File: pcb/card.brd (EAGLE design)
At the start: 84.8 x 54 mm, 18 parts, among them IC1 74HC14D, IC2 W25X32, Q1 BC817

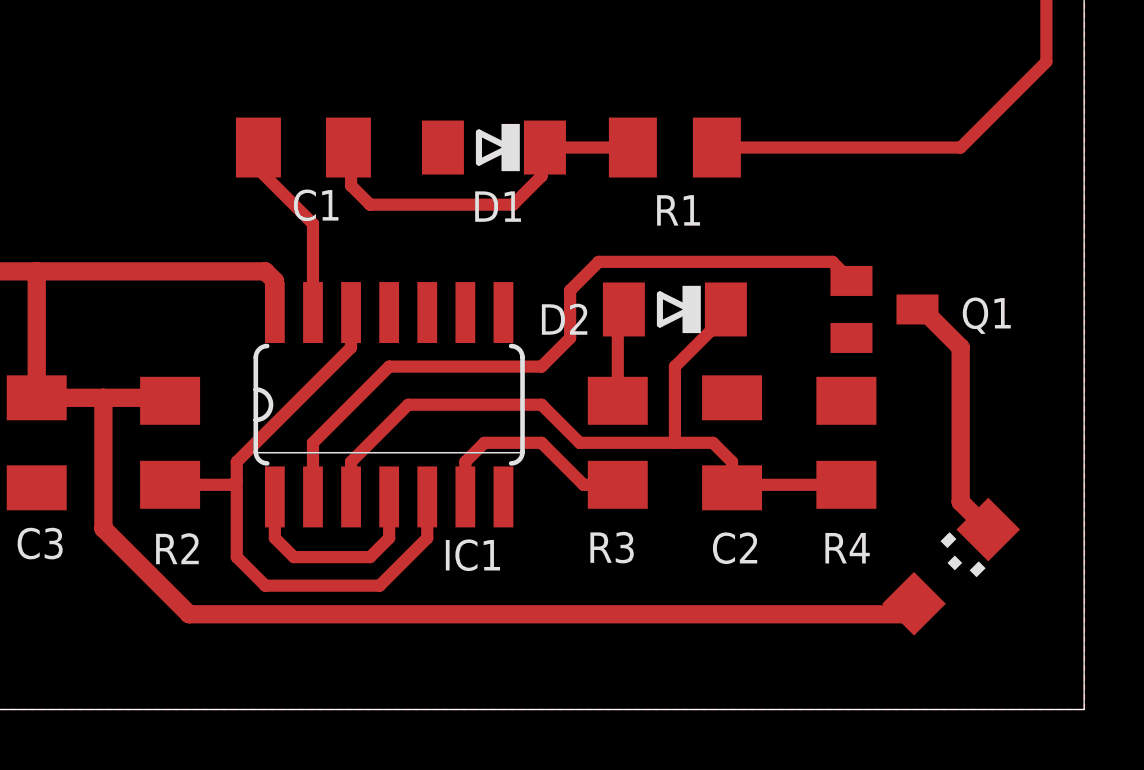
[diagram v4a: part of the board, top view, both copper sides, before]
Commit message: Added a current limitting resistor to the LED.
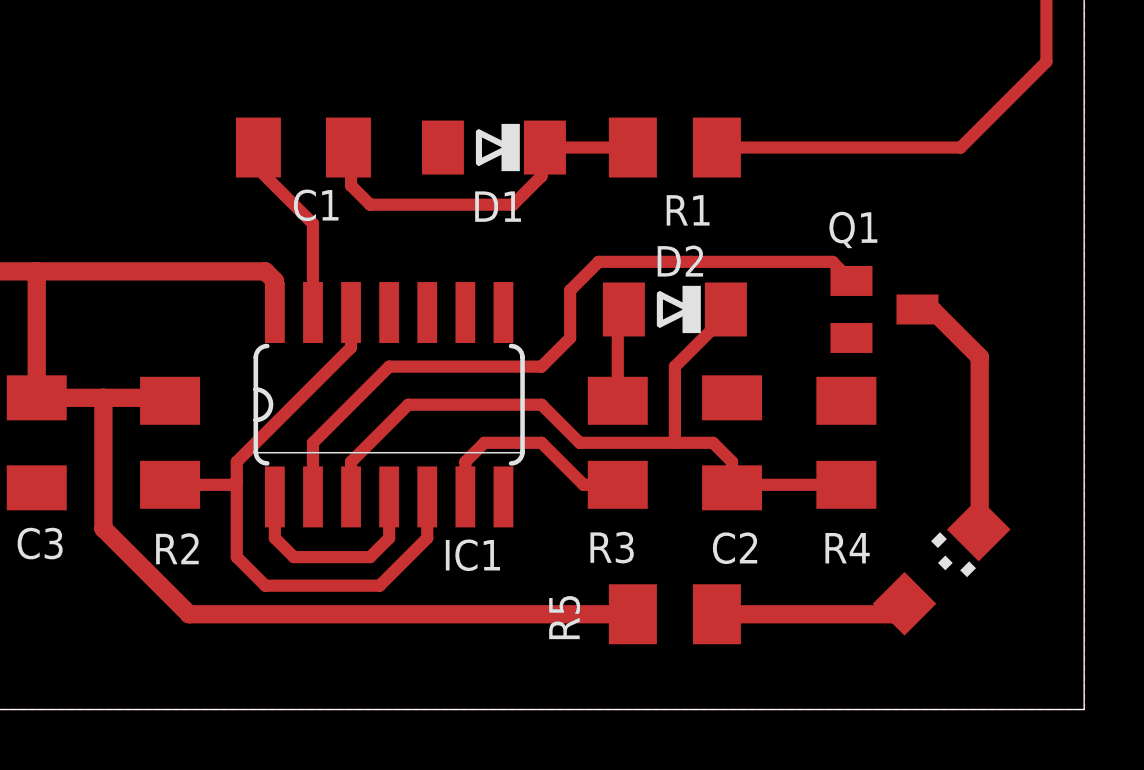
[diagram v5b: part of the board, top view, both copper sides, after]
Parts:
- added R5: 470R, resistor:M1206
- moved LED 0.32 mm to (80.0, 4.76)
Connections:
- new net N$3: LED.A, R5.2
- net VCC: now also R5.1; no longer LED.A
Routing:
- net VCC: track 77.7 -> 67.9 mm
- net N$3: track 0.00 -> 6.40 mm
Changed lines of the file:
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@@
 </element>
 <element name="D2" library="diode" package="MINIMELF" value="" x="71.12" y="13.335" smashed="yes" rot="R180">
-<attribute name="NAME" x="68.326" y="13.509515625" size="1.016" layer="25" rot="R180"/>
+<attribute name="NAME" x="70.4215" y="14.430484375" size="1.016" layer="25"/>
 <attribute name="VALUE" x="72.771" y="15.748" size="1.27" layer="27" rot="R180"/>
 </element>
@@
 <attribute name="NAME" x="65.405" y="5.6515" size="1.016" layer="25" ratio="10" rot="R180"/>
 </element>
-<element name="LED" library="led" package="CHIPLED_1206" value="" x="80.3275" y="4.7625" smashed="yes" rot="R315">
-<attribute name="VALUE" x="81.225525" y="2.068425" size="1.27" layer="27" rot="R45"/>
+<element name="LED" library="led" package="CHIPLED_1206" value="" x="80.01" y="4.7625" smashed="yes" rot="R315">
+<attribute name="VALUE" x="80.908021875" y="2.068425" size="1.27" layer="27" rot="R45"/>
 </element>
 <element name="Q1" library="transistor" package="SOT23-BEC" value="BC817" x="78.105" y="13.335" smashed="yes" rot="R270">
-<attribute name="NAME" x="80.645" y="12.7" size="1.016" layer="25"/>
+<attribute name="NAME" x="76.2" y="15.5575" size="1.016" layer="25"/>
 </element>
 <element name="R1" library="resistor" package="M1206" value="470k" x="71.12" y="18.7325" smashed="yes">
-<attribute name="NAME" x="72.0725" y="17.145" size="1.016" layer="25" rot="R180"/>
+<attribute name="NAME" x="72.39" y="17.145" size="1.016" layer="25" rot="R180"/>
 </element>
 <element name="R3" library="resistor" package="M1206" value="100k" x="69.215" y="8.89" smashed="yes" rot="R270">
@@
 <attribute name="NAME" x="66.1035" y="17.272" size="1.016" layer="25" rot="R180"/>
 <attribute name="VALUE" x="66.7385" y="21.1455" size="1.27" layer="27" rot="R180"/>
+</element>
+<element name="R5" library="resistor" package="M1206" value="470R" x="71.12" y="3.175" smashed="yes">
+<attribute name="NAME" x="67.945" y="2.2225" size="1.016" layer="25" rot="R90"/>
 </element>
 </elements>
@@
 <contactref element="IC1" pad="14"/>
 <contactref element="R2" pad="2"/>
-<contactref element="LED" pad="A"/>
 <contactref element="C3" pad="2"/>
 <wire x1="57.785" y1="12.7" x2="57.785" y2="13.2334" width="0.4064" layer="1"/>
 <contactref element="BAT" pad="+@2" route="any" routetag="G$1.+"/>
 <contactref element="BAT" pad="+@1" route="any" routetag="G$1.+"/>
-<wire x1="79.122625" y1="3.175" x2="79.0900625" y2="3.5250625" width="0.4064" layer="1"/>
 <contactref element="IC2" pad="8"/>
 <contactref element="IC2" pad="7"/>
@@
 <wire x1="52.07" y1="10.39" x2="54.1925" y2="10.39" width="0.6096" layer="1"/>
 <wire x1="54.1925" y1="10.39" x2="54.2925" y2="10.29" width="0.6096" layer="1"/>
-<wire x1="79.122625" y1="3.175" x2="54.9275" y2="3.175" width="0.6096" layer="1"/>
 <wire x1="54.9275" y1="3.175" x2="52.07" y2="6.0325" width="0.6096" layer="1"/>
 <wire x1="52.07" y1="6.0325" x2="52.07" y2="10.39" width="0.6096" layer="1"/>
+<contactref element="R5" pad="1"/>
+<wire x1="69.72" y1="3.175" x2="54.9275" y2="3.175" width="0.6096" layer="1"/>
 </signal>
 <signal name="N$2">
@@
 <wire x1="67.6275" y1="13.97" x2="68.58" y2="14.9225" width="0.4064" layer="1"/>
 </signal>
-<signal name="N$13">
-<contactref element="Q1" pad="C"/>
-<contactref element="LED" pad="C"/>
-<wire x1="79.205" y1="13.335" x2="79.375" y2="13.335" width="0.4064" layer="1"/>
-<wire x1="79.375" y1="13.335" x2="80.645" y2="12.065" width="0.6096" layer="1"/>
-<wire x1="80.645" y1="12.065" x2="80.645" y2="6.91986875" width="0.6096" layer="1"/>
-<wire x1="80.645" y1="6.91986875" x2="81.564934375" y2="5.999934375" width="0.6096" layer="1"/>
-</signal>
 <signal name="ANT">
 <contactref element="R1" pad="2"/>
@@
 <wire x1="59.055" y1="16.1925" x2="59.055" y2="13.2334" width="0.4064" layer="1"/>
 </signal>
+<signal name="N$3">
+<contactref element="LED" pad="A"/>
+<contactref element="R5" pad="2"/>
+<wire x1="72.52" y1="3.175" x2="78.4225" y2="3.175" width="0.6096" layer="1"/>
+<wire x1="78.4225" y1="3.175" x2="78.7725625" y2="3.5250625" width="0.6096" layer="1"/>
+</signal>
+<signal name="N$4">
+<contactref element="Q1" pad="C"/>
+<contactref element="LED" pad="C"/>
+<wire x1="79.205" y1="13.335" x2="79.6925" y2="13.335" width="0.6096" layer="1"/>
+<wire x1="79.6925" y1="13.335" x2="81.28" y2="11.7475" width="0.6096" layer="1"/>
+<wire x1="81.28" y1="11.7475" x2="81.28" y2="6.0325" width="0.6096" layer="1"/>
+<wire x1="81.28" y1="6.0325" x2="81.247434375" y2="5.999934375" width="0.6096" layer="1"/>
+</signal>
 </signals>

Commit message: Swapped the NPN tranny for a MOSFET.
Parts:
- Q1: value BC817 -> 2N7002; device transistor:SOT23-BEC -> transistors:SOT-23
- moved Q1 0.45 mm to (77.8, 13.7)
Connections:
- net GND: now also Q1.2; no longer Q1.E
- net N$12: now also Q1.1; no longer Q1.B
- net N$4: now also Q1.3; no longer Q1.C
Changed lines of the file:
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@@
 <attribute name="VALUE" x="80.908021875" y="2.068425" size="1.27" layer="27" rot="R45"/>
-</element>
-<element name="Q1" library="transistor" package="SOT23-BEC" value="BC817" x="78.105" y="13.335" smashed="yes" rot="R270">
-<attribute name="NAME" x="76.2" y="15.5575" size="1.016" layer="25"/>
 </element>
 <element name="R1" library="resistor" package="M1206" value="470k" x="71.12" y="18.7325" smashed="yes">
@@
 </element>
 <element name="R5" library="resistor" package="M1206" value="470R" x="71.12" y="3.175" smashed="yes">
-<attribute name="NAME" x="67.945" y="2.2225" size="1.016" layer="25" rot="R90"/>
+<attribute name="NAME" x="68.58" y="3.175" size="1.016" layer="25" rot="R180"/>
+</element>
+<element name="Q1" library="transistors" package="SOT-23" value="2N7002" x="77.7875" y="13.6525" smashed="yes" rot="R270">
+<attribute name="NAME" x="76.962" y="15.6845" size="1.016" layer="21"/>
 </element>
 </elements>
@@
 <contactref element="R4" pad="2"/>
 <contactref element="C2" pad="2"/>
-<contactref element="Q1" pad="E"/>
 <contactref element="C3" pad="1"/>
 <polygon width="0.4064" layer="1" isolate="0.6096" orphans="yes">
@@
 <contactref element="IC2" pad="3"/>
 <contactref element="D1" pad="A"/>
+<contactref element="Q1" pad="2"/>
 </signal>
 <signal name="VCC">
@@
 <signal name="N$12">
 <contactref element="IC1" pad="2"/>
-<contactref element="Q1" pad="B"/>
 <wire x1="59.055" y1="7.0866" x2="59.055" y2="8.89" width="0.4064" layer="1"/>
 <wire x1="59.055" y1="8.89" x2="61.595" y2="11.43" width="0.4064" layer="1"/>
 <wire x1="61.595" y1="11.43" x2="66.675" y2="11.43" width="0.4064" layer="1"/>
-<wire x1="68.58" y1="14.9225" x2="76.3725" y2="14.9225" width="0.4064" layer="1"/>
-<wire x1="76.3725" y1="14.9225" x2="77.005" y2="14.285" width="0.4064" layer="1"/>
 <wire x1="66.675" y1="11.43" x2="67.6275" y2="12.3825" width="0.4064" layer="1"/>
 <wire x1="67.6275" y1="12.3825" x2="67.6275" y2="13.97" width="0.4064" layer="1"/>
 <wire x1="67.6275" y1="13.97" x2="68.58" y2="14.9225" width="0.4064" layer="1"/>
+<contactref element="Q1" pad="1"/>
+<wire x1="68.58" y1="14.9225" x2="76.3953" y2="14.9225" width="0.4064" layer="1"/>
+<wire x1="76.3953" y1="14.9225" x2="76.6861" y2="14.6317" width="0.4064" layer="1"/>
 </signal>
 <signal name="ANT">
@@
 </signal>
 <signal name="N$4">
-<contactref element="Q1" pad="C"/>
 <contactref element="LED" pad="C"/>
-<wire x1="79.205" y1="13.335" x2="79.6925" y2="13.335" width="0.6096" layer="1"/>
-<wire x1="79.6925" y1="13.335" x2="81.28" y2="11.7475" width="0.6096" layer="1"/>
+<wire x1="79.4004" y1="13.6271" x2="81.28" y2="11.7475" width="0.6096" layer="1"/>
 <wire x1="81.28" y1="11.7475" x2="81.28" y2="6.0325" width="0.6096" layer="1"/>
 <wire x1="81.28" y1="6.0325" x2="81.247434375" y2="5.999934375" width="0.6096" layer="1"/>
+<contactref element="Q1" pad="3"/>
+<wire x1="78.8543" y1="13.6271" x2="79.4004" y2="13.6271" width="0.6096" layer="1"/>
 </signal>
 </signals>

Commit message: Compacted & improved the design.
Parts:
- moved D1 15.4 mm to (79.4, 13.0), turned to 0 degrees
- moved C1 14.5 mm to (73.0, 16.5)
- moved R5 13.9 mm to (67.3, 16.5)
- moved Q1 10.1 mm to (73.0, 4.76)
- moved C3 9.47 mm to (59.1, 6.67)
- moved R1 8.55 mm to (79.4, 16.5)
- moved MISO 7.01 mm to (43.2, 5.40), turned to 180 degrees
- moved GND 6.48 mm to (37.5, 5.40), turned to 180 degrees
- moved MOSI 5.68 mm to (41.3, 5.40), turned to 180 degrees
- moved SCLK 5.46 mm to (39.4, 5.40), turned to 180 degrees
- moved IC1 4.94 mm to (65.1, 6.67)
- moved R3 4.55 mm to (67.3, 13.0), turned to 180 degrees
- moved IC2 3.14 mm to (40.3, 11.1), turned to 180 degrees
- moved R2 2.73 mm to (55.9, 6.67)
- moved R4 2.62 mm to (79.4, 9.53), turned to 0 degrees
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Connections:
- net GND: now also IC1.1, IC1.3; no longer IC1.11, IC1.9
- net N$11: now also IC1.5, IC1.8; no longer IC1.1, IC1.4
- net N$12: now also IC1.6; no longer IC1.2
- net N$5: now also IC1.11; no longer IC1.5
- net N$6: now also IC1.10; no longer IC1.6
- net N$8: now also IC1.9; no longer IC1.3
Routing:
- net N$3: track 6.40 -> 24.5 mm
- net N$12: track 23.0 -> 6.47 mm
- net VCC: track 67.9 -> 55.1 mm
- net N$5: track 21.3 -> 11.9 mm
- net N$8: track 25.6 -> 16.8 mm
- net N$1: track 6.25 -> 14.4 mm
- net ANT: track 81.4 -> 75.5 mm
- net N$2: track 12.2 -> 7.01 mm
- net N$4: track 8.97 -> 4.42 mm
- net N$6: track 7.83 -> 3.46 mm
- net N$11: track 8.15 -> 7.20 mm
- net N$10: track 7.88 -> 7.25 mm
- net N$9: track 9.94 -> 9.31 mm
- net N$88: track 7.40 -> 6.77 mm
- net N$94: track 0.00 -> 0.50 mm
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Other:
- board text added: "AC detector"
- board text removed: "detector"

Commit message: Added a back side to the card.
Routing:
- net N$95: track 0.00 -> 3.49 mm
- net N$159: track 0.00 -> 3.49 mm
- net N$115: track 0.00 -> 3.49 mm
- net N$161: track 0.00 -> 2.86 mm
- net N$129: track 0.00 -> 2.86 mm
- net N$105: track 0.00 -> 2.86 mm
- net N$160: track 0.00 -> 2.38 mm
- net N$130: track 0.00 -> 2.38 mm
- net N$128: track 0.00 -> 2.38 mm
- net N$110: track 0.00 -> 2.38 mm
- net N$100: track 0.00 -> 2.38 mm
- net N$96: track 0.00 -> 1.75 mm
- net N$164: track 0.00 -> 1.75 mm
- net N$163: track 0.00 -> 1.75 mm
- net N$132: track 0.00 -> 1.75 mm
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- added copper zone on layer 16, net GND
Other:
- board text added: "WARNING: Do not use with exposed main AC wiring. The issuer of this business card takes no responsibility for any injuries or damages caused by improper use of this device."
